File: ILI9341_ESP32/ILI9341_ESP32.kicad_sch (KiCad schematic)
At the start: 87 parts, among them J1 USB_C_Receptacle_USB2.0_16P, J10 Conn_01x01_Pin, J9 Conn_01x01_Pin, Q1 BC817, Q3 BC817, Q4 BC817, SW1 SS-12F23-G040, SW7 SW_Push, SW8 SW_Push, U1 HE6250xx, U10 CH340K, U11 ESP32-WROVER-E-N8R8, U2 XM5062S, U3 PAM8406D, U4 MAX98357AETE+T, U7 02FVS3

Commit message: zwischenstand v2
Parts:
- removed C12, C15, C18, C5: 4µ7, Capacitor_SMD:C_1206_3216Metric, symbol Device:C
- removed C13, C14: 100n, Capacitor_SMD:C_1206_3216Metric, symbol Device:C
- removed C16, C17, C6, C7: 220p, Capacitor_SMD:C_0603_1608Metric, symbol Device:C
- removed C27: 470µ, symbol Device:C_Polarized
- removed D1: LED, LED_SMD:LED_0603_1608Metric, symbol Device:LED
- removed FB1, FB2, FB3, FB4, FB5, FB8, FB9: FerriteBead_Small, Inductor_SMD:L_0805_2012Metric, symbol Device:FerriteBead_Small
- removed Q3: BC817, Package_TO_SOT_SMD:SOT-323_SC-70, symbol Transistor_BJT:BC817
- removed R1, R2, R22, R32: 100K, Resistor_SMD:R_0603_1608Metric_Pad0.98x0.95mm_HandSolder, symbol Device:R
- removed R10, R11, R14, R20, R21, R8: 5K1, Resistor_SMD:R_0603_1608Metric, symbol Device:R
- removed R16, R17, R18, R19, R3, R35, R36, R37, R38, R39, R40, R41, R42: 5K1, Resistor_SMD:R_0603_1608Metric_Pad0.98x0.95mm_HandSolder, symbol Device:R
- removed SW7, SW8: SW_Push, TheBrutzlers_Lib:RubberpadButton_250µ_250µ, symbol Switch:SW_Push
- removed U11: ESP32-WROVER-E-N8R8, easyeda2kicad:WIFI-SMD_ESP32-WROVER-IE8MB, symbol easyeda2kicad:ESP32-WROVER-E-N8R8
- removed U3: PAM8406D, Package_SO:SOP-16_3.9x9.9mm_P1.27mm, symbol Amplifier_Audio:PAM8406D
- removed U4: MAX98357AETE+T, Package_DFN_QFN:QFN-16-1EP_3x3mm_P0.5mm_EP1.45x1.45mm, symbol MAX98357AETE_T:MAX98357AETE+T
- C28: footprint (none) -> Capacitor_Tantalum_SMD:CP_EIA-7343-43_Kemet-X; LCSC (none) -> C724264
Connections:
- net GND: now also J1.A1 (GND), J1.A12 (GND), J1.B1 (GND), J1.B12 (GND), J1.S1 (SHIELD)
- no-connect marks 14 -> 3
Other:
- moved on the sheet: C28, C4, C8, L1, R12, R13, R9, U2, U7

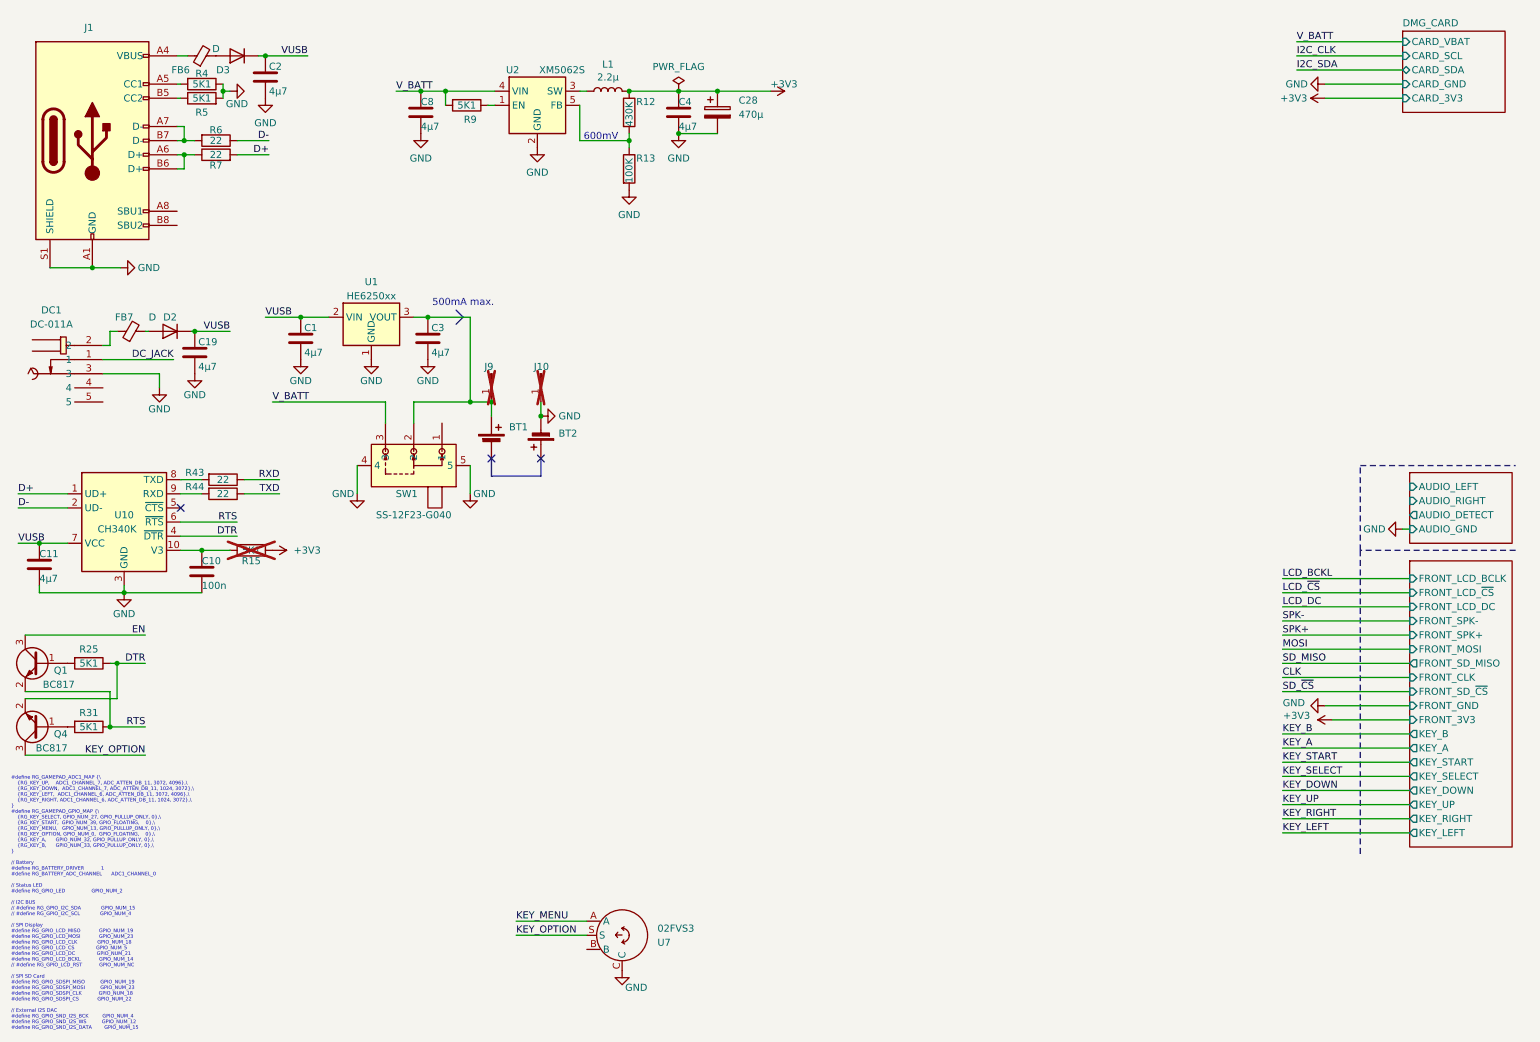
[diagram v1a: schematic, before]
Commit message: Update PCB and add RGB
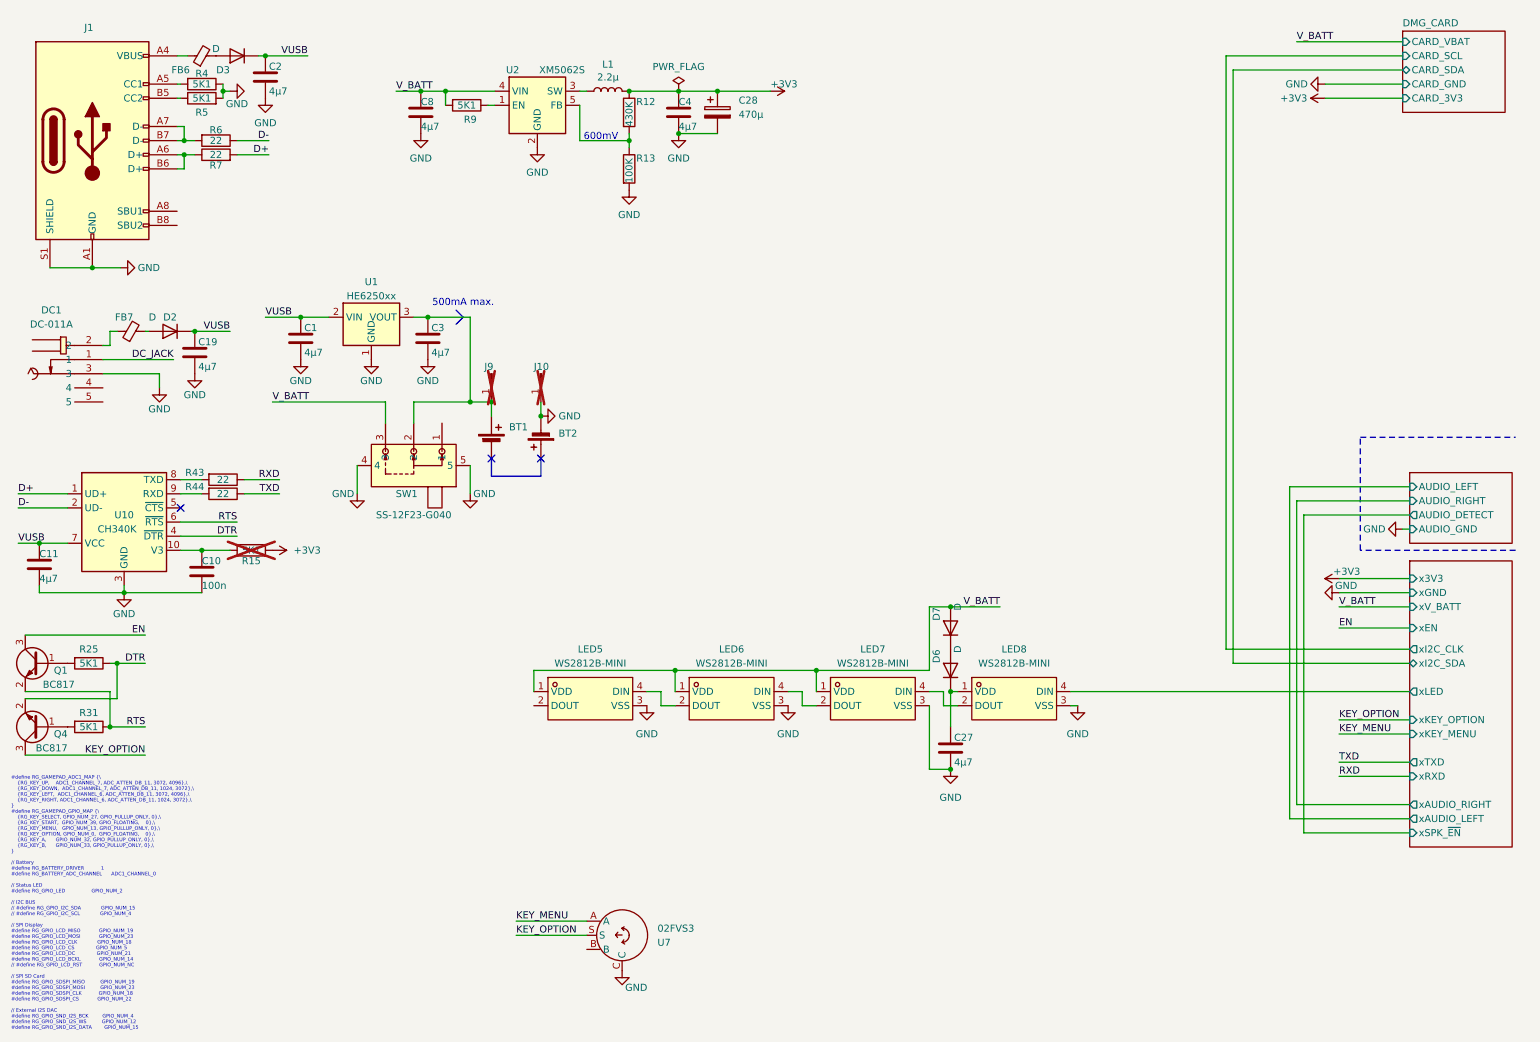
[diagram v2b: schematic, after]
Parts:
- added C27: 4µ7, Capacitor_SMD:C_1206_3216Metric, symbol Device:C
- added D6, D7: D, Diode_SMD:Nexperia_CFP3_SOD-123W, symbol Device:D
- added LED5, LED6, LED7, LED8: WS2812B-MINI, easyeda2kicad:LED-SMD_4P-L3.5-W3.5-TL_WS2812B, symbol easyeda2kicad:WS2812B-MINI
- C10: footprint Capacitor_SMD:C_1206_3216Metric -> Capacitor_SMD:C_0603_1608Metric; LCSC C464972 -> (none)
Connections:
- net GND: now also C27.2, LED5.3 (VSS), LED6.3 (VSS), LED7.3 (VSS), LED8.3 (VSS)
- net V_BATT: now also D7.2 (A), LED5.1 (VDD), LED6.1 (VDD), LED7.1 (VDD)
- new net: LED6.4 (DIN), LED7.2 (DOUT)
- new net: LED7.4 (DIN), LED8.2 (DOUT)
- new net: LED5.4 (DIN), LED6.2 (DOUT)
- new net: D6.2 (A), D7.1 (K)
- new net: C27.1, D6.1 (K), LED8.1 (VDD)
- new net FRONT_BUTTONS/xLED: LED8.4 (DIN)
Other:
- sheet FRONT_BUTTONS ports: added x3V3, xAUDIO_LEFT, xAUDIO_RIGHT, xEN, xGND, xI2C_CLK, xI2C_SDA, xKEY_MENU, xKEY_OPTION, xLED, xRXD, xSPK_~{EN}, xTXD, xV_BATT; removed FRONT_3V3, FRONT_CLK, FRONT_GND, FRONT_LCD_BCLK, FRONT_LCD_DC, FRONT_LCD_~{CS}, FRONT_MOSI, FRONT_SD_MISO, FRONT_SD_~{CS}, FRONT_SPK+, FRONT_SPK-, KEY_A, KEY_B, KEY_DOWN, KEY_LEFT, KEY_RIGHT, KEY_SELECT, KEY_START, KEY_UP

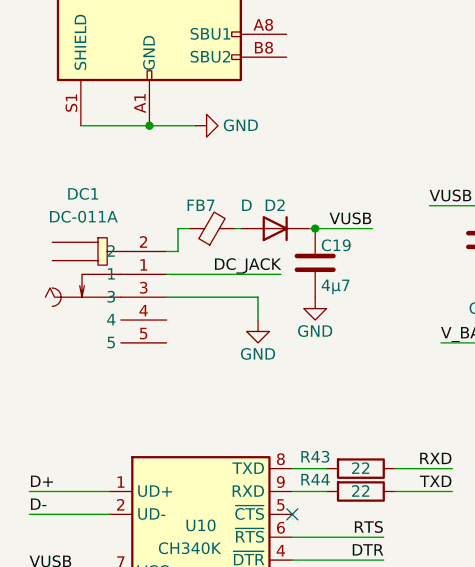
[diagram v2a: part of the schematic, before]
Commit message: update nimh charger and battery protection
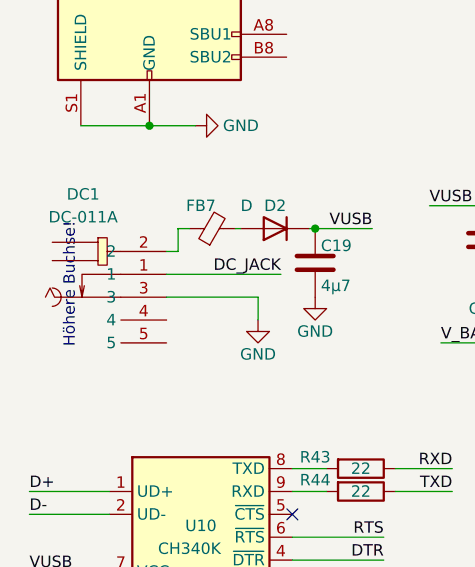
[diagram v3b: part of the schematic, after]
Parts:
- DC1: LCSC (none) -> C480366; LCSC Part C480366 -> (none)
- LED5, LED6, LED7, LED8: LCSC (none) -> C527089; LCSC Part C527089 -> (none)
- SW1: LCSC (none) -> C2848932; LCSC Part C2848932 -> (none)
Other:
- note added: "Höhere Buchse!"
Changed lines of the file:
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@@
 		)
 	)
+	(text "Höhere Buchse!"
+		(exclude_from_sim no)
+		(at 19.685 77.47 90)
+		(effects
+			(font
+				(size 1.27 1.27)
+			)
+		)
+	)
 	(label "VUSB"
 		(at 15.24 109.22 0)
@@
 			)
 		)
-		(property "LCSC Part" "C480366"
+		(property "LCSC Part" ""
 			(at 24.13 93.98 0)
 			(effects
@@
 			)
 		)
+		(property "LCSC" "C480366"
+			(at 24.13 76.2 0)
+			(effects
+				(font
+					(size 1.27 1.27)
+				)
+				(hide yes)
+			)
+		)
 		(pin "3"
 		)
@@
 			)
 		)
-		(property "LCSC Part" "C527089"
+		(property "LCSC Part" ""
 			(at 168.91 151.13 0)
 			(effects
@@
 			)
 		)
+		(property "LCSC" "C527089"
+			(at 168.91 137.16 0)
+			(effects
+				(font
+					(size 1.27 1.27)
+				)
+				(hide yes)
+			)
+		)
 		(pin "2"
 		)
@@
 			)
 		)
-		(property "LCSC Part" "C527089"
+		(property "LCSC Part" ""
 			(at 118.11 151.13 0)
 			(effects
@@
 			)
 		)
+		(property "LCSC" "C527089"
+			(at 118.11 137.16 0)
+			(effects
+				(font
+					(size 1.27 1.27)
+				)
+				(hide yes)
+			)
+		)
 		(pin "2"
 		)
@@
 			)
 		)
-		(property "LCSC Part" "C527089"
+		(property "LCSC Part" ""
 			(at 143.51 151.13 0)
 			(effects
@@
 			)
 		)
+		(property "LCSC" "C527089"
+			(at 143.51 137.16 0)
+			(effects
+				(font
+					(size 1.27 1.27)
+				)
+				(hide yes)
+			)
+		)
 		(pin "2"
 		)
@@
 			)
 		)
-		(property "LCSC Part" "C527089"
+		(property "LCSC Part" ""
 			(at 194.31 151.13 0)
 			(effects
@@
 			)
 		)
+		(property "LCSC" "C527089"
+			(at 194.31 137.16 0)
+			(effects
+				(font
+					(size 1.27 1.27)
+				)
+				(hide yes)
+			)
+		)
 		(pin "2"
 		)
@@
 			)
 		)
-		(property "LCSC Part" "C2848932"
+		(property "LCSC Part" ""
 			(at 86.36 77.47 0)
 			(effects
@@
 			(at 86.36 95.25 0)
 			(effects
+				(font
+					(size 1.27 1.27)
+				)
+				(hide yes)
+			)
+		)
+		(property "LCSC" "C2848932"
+			(at 86.36 95.25 0)
+			(effects

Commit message: ordered Version
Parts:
- removed U1: HE6250xx, Package_TO_SOT_SMD:SOT-89-3, symbol Regulator_Linear:HT75xx-1-SOT89
- added C32, C33: 4µ7, Capacitor_SMD:C_1206_3216Metric, symbol Device:C
- added D4: LED, LED_SMD:LED_0603_1608Metric, symbol Device:LED
- added L2: 2.2µ, Inductor_SMD:L_1210_3225Metric_Pad1.42x2.65mm_HandSolder, symbol Device:L
- added Q10: PMOS, Package_TO_SOT_SMD:SOT-323_SC-70, symbol Device:Q_PMOS_GSD
- added Q9: BC817, Package_TO_SOT_SMD:SOT-323_SC-70, symbol Transistor_BJT:BC817
- added R48, R49, R52: 15K, Resistor_SMD:R_0603_1608Metric, symbol Device:R
- added R50, R51, R55: 1K1, Resistor_SMD:R_0603_1608Metric, symbol Device:R
- added R53, R54: 10K, Resistor_SMD:R_0603_1608Metric, symbol Device:R
- added R57: 5K1, Resistor_SMD:R_0603_1608Metric, symbol Device:R
- added R58, R59: 100K, Resistor_SMD:R_0603_1608Metric, symbol Device:R
- added R60: 510K, Resistor_SMD:R_0603_1608Metric, symbol Device:R
- added U1: TPS61028DRCR, easyeda2kicad:VSON-10_L3.0-W3.0-P0.50-TL-EP-1, symbol easyeda2kicad:TPS61028DRCR
- added U9: BQ25171QWDRCRQ1, easyeda2kicad:VSON-10_L3.0-W3.0-P0.50-BL-EP1.65, symbol easyeda2kicad:BQ25171QWDRCRQ1
- BT1, BT2, C1, C10, C11, C19, C2, C27, C3, C4, C8, D2, D3, D6, D7, DC1, FB6, FB7, J1, L1, Q1, Q4, SW1, U10, U2, U7: SOURCED jop -> (none)
- C28: SOURCED (none) -> card
- R12, R13, R25, R31, R4, R43, R44, R5, R6, R7: footprint Resistor_SMD:R_0603_1608Metric_Pad0.98x0.95mm_HandSolder -> Resistor_SMD:R_0603_1608Metric; SOURCED jop -> (none)
- R15: footprint Resistor_SMD:R_0603_1608Metric_Pad0.98x0.95mm_HandSolder -> Resistor_SMD:R_0603_1608Metric
- R9: value 5K1 -> 100K; footprint Resistor_SMD:R_0603_1608Metric_Pad0.98x0.95mm_HandSolder -> Resistor_SMD:R_0603_1608Metric; LCSC C26000 -> C15458; SOURCED jop -> (none)
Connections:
- net GND: now also R9.2, C32.1, C33.1, Q9.2 (E), R48.1, R49.1, R50.2, R51.1, R53.2, R54.1, R59.2, U1.10 (PGND), U1.11 (EP), U1.5 (GND), U1.7 (LBI), U1.8 (PS), U9.11 (EP), U9.5 (GND)
- net VUSB: now also L2.1, R57.1, U1.1 (EN), U1.6 (VBAT)
- net V_BATT: now also Q10.2 (S), R58.1, R60.1; no longer R9.2
- net at BT1.1 (+), C3.1, J9.1 (Pin_1)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: now also U9.10 (OUT)
- net at R9.1, U2.1 (EN): now also Q10.3 (D)
- new net: R54.2, R55.1, U9.3 (~{CE})
- new net: C32.2, C33.2, R52.2, U1.2 (VOUT), U9.1 (IN)
- new net: R51.2, R52.1, U1.3 (FB)
- new net: L2.2, U1.9 (SW)
- new net: Q9.1 (B), R59.1, R60.2
- new net: Q10.1 (G), Q9.3 (C), R58.2
- new net: R50.1, U9.2 (ISET)
- new net: R53.1, U9.4 (TS)
- new net: R49.2, U9.6 (CHM_TMR)
- new net: R48.2, U9.9 (VSET)
- new net CHARGER_EN: R55.2
- new net STAT1: D4.2 (A), R57.2, U9.7 (STAT1)
- new net STAT2: D4.1 (K), U9.8 (STAT2)
- no-connect marks 3 -> 4
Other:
- sheet DMG_CARD ports: added CHARGER_EN; removed none
- note added: "12h timeout"
- note added: "280mA"
- note added: "280mA max."
- note added: "4cells"
- note added: "500mV"
- note added: "650mV"
- note added: "7,3V"
- note added: "HIGH"
- note added: "LOW"
- note removed: "500mA max."
- moved on the sheet: BT1, BT2, C1, C28, C3, C4, C8, J10, J9, L1, R12, R13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
